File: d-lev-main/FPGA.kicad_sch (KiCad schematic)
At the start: 24 parts, among them J2 Tag-Connect TC2030-NL, SW10 SW_Push, SW9 SW_Push, U2 25LCxxx, U3 AC608

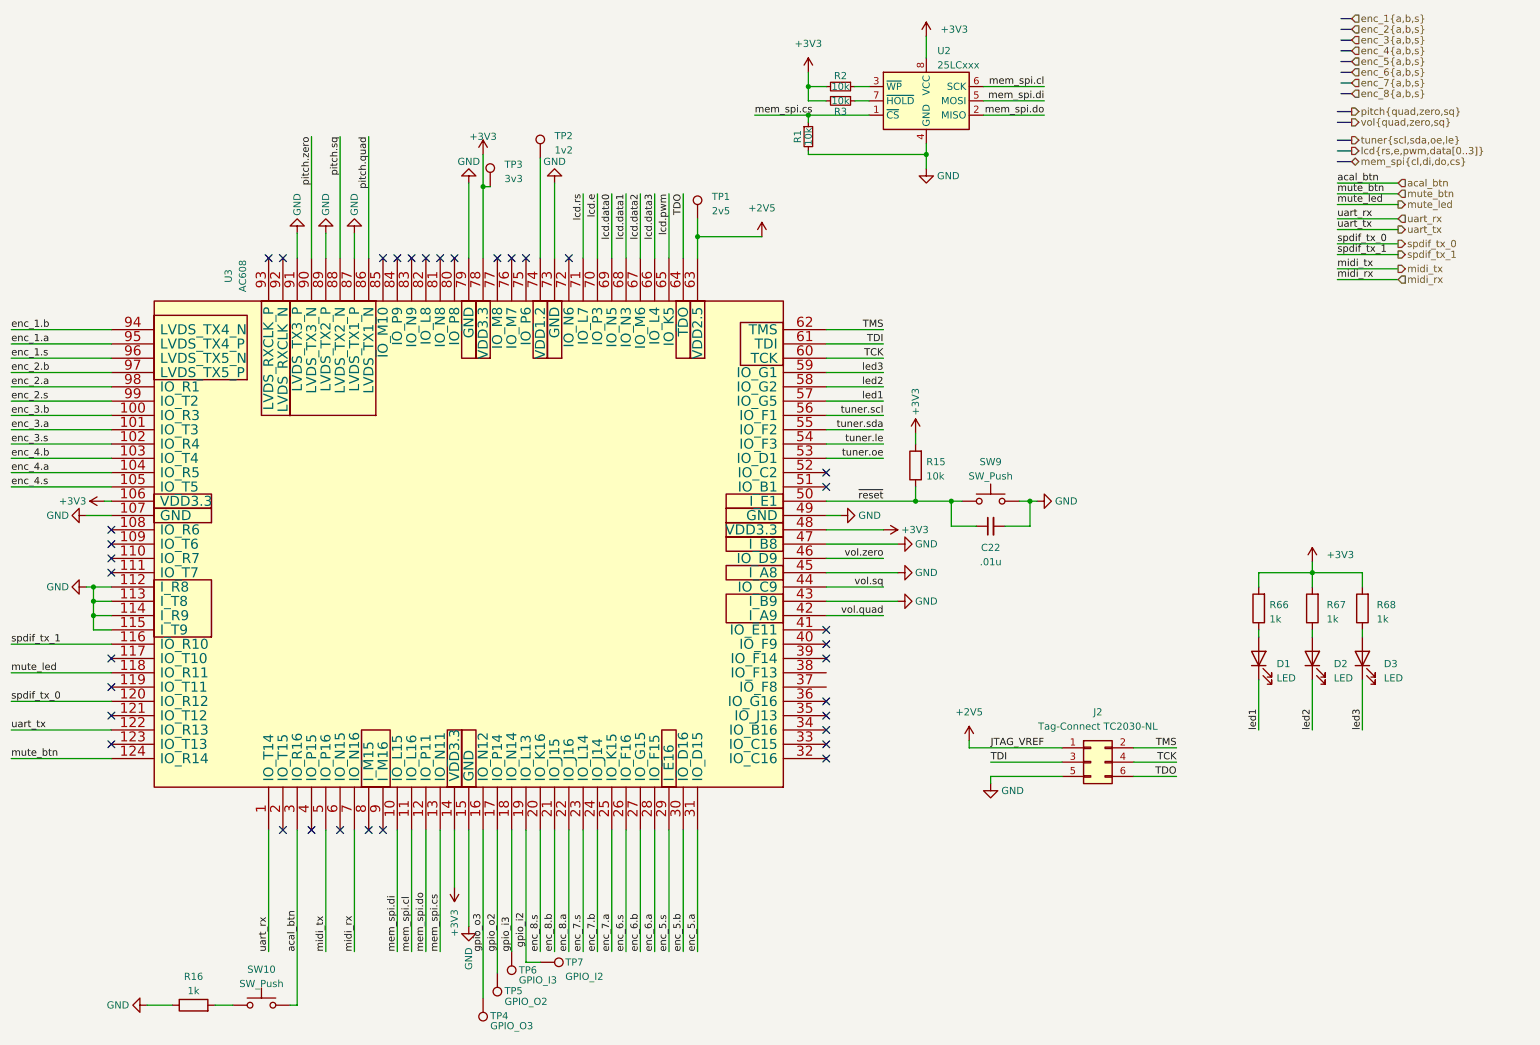
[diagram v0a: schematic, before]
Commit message: round tracks and teardrops
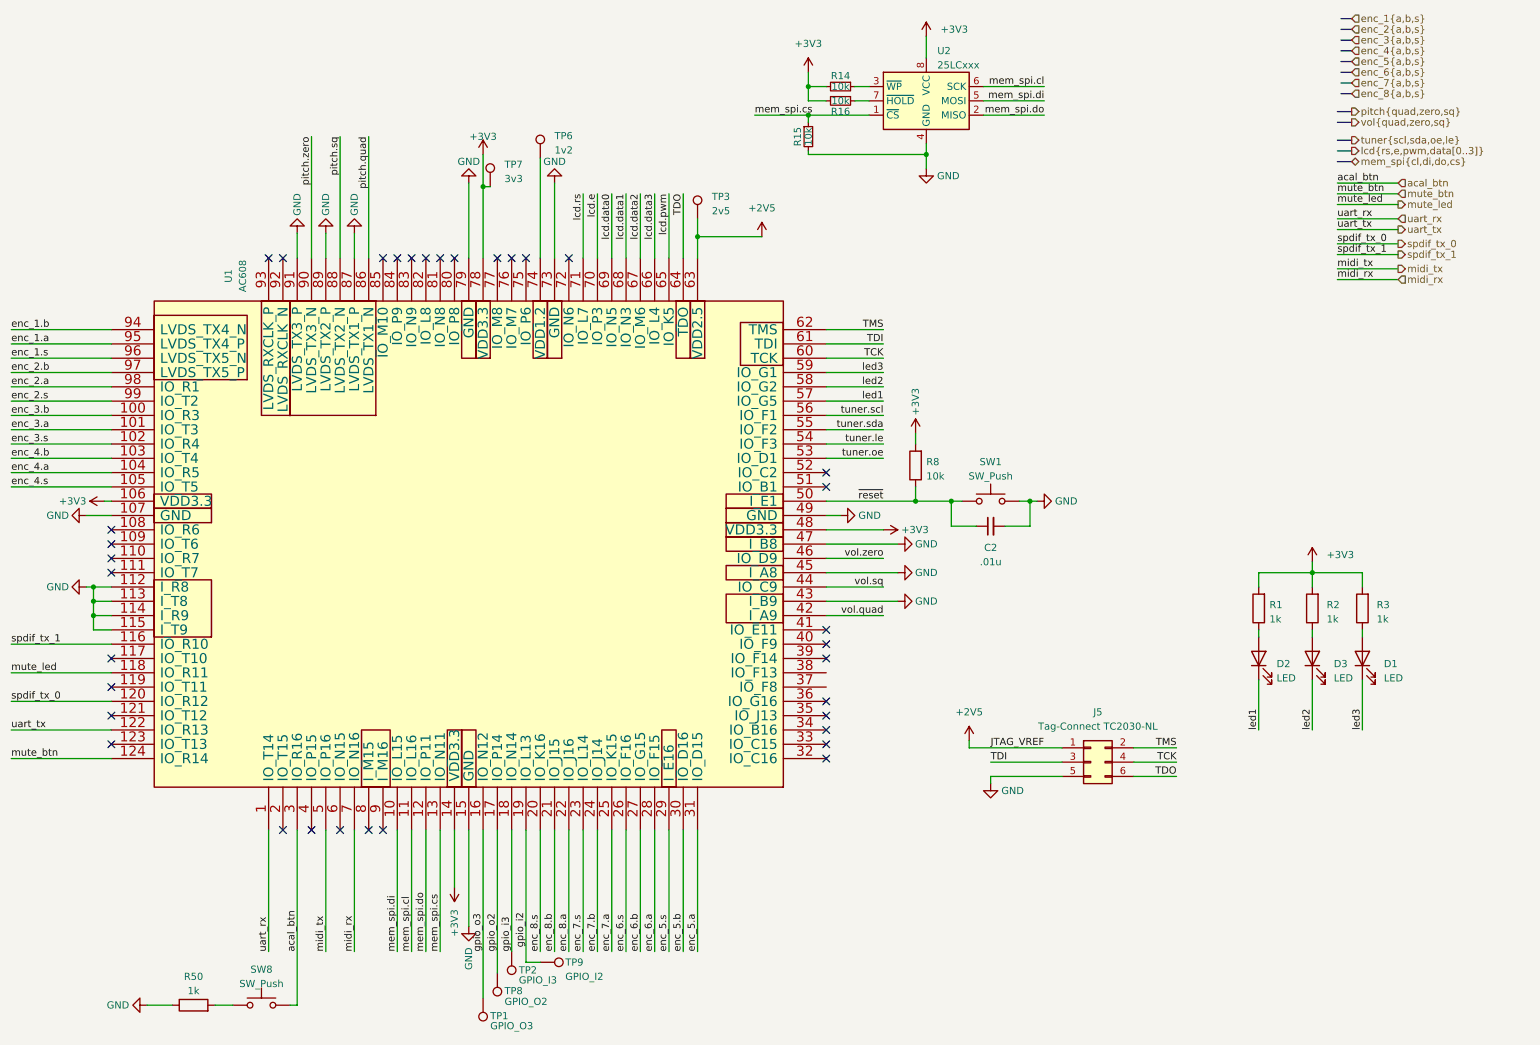
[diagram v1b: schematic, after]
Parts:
- renumbered C22 to C2, D3 to D1, D1 to D2, D2 to D3, J2 to J5, R66 to R1, R2 to R14, R1 to R15, R3 to R16, R67 to R2, R68 to R3, R16 to R50, R15 to R8, SW9 to SW1, SW10 to SW8, TP4 to TP1, TP6 to TP2, TP1 to TP3, TP2 to TP6, TP3 to TP7, TP5 to TP8, TP7 to TP9, U3 to U1

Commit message: many board updates
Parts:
- removed R50: 1k, Resistor_SMD:R_0603_1608Metric, symbol Device:R
- removed SW8: SW_Push, Button_Switch_SMD:SW_SPST_B3U-1000P, symbol Switch:SW_Push
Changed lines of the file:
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@@
-    (stroke (width 0) (type default))
-  )
-  (wire (pts (xy 43.18 191.77) (xy 47.625 191.77))
     (stroke (width 0) (type default))
   )
@@
     (stroke (width 0) (type default))
   )
-  (wire (pts (xy 69.85 191.77) (xy 69.85 160.655))
+  (wire (pts (xy 69.85 182.245) (xy 69.85 160.655))
     (stroke (width 0) (type default))
   )
@@
     (stroke (width 0) (type default))
   )
-  (wire (pts (xy 68.58 191.77) (xy 69.85 191.77))
-    (stroke (width 0) (type default))
-  )
   (wire (pts (xy 19.05 142.875) (xy 36.83 142.875))
     (stroke (width 0) (type default))
@@
   )
   (wire (pts (xy 80.01 59.055) (xy 80.01 54.61))
-    (stroke (width 0) (type default))
-  )
-  (wire (pts (xy 55.245 191.77) (xy 58.42 191.77))
     (stroke (width 0) (type default))
   )
@@
         (path "/eb5e8bfd-9871-4528-bf57-58851bf63907/acdfb54c-8449-4fbe-9778-47a925c872ef"
           (reference "TP8") (unit 1)
-        )
-      )
-    )
-  )
-  (symbol (lib_id "Switch:SW_Push") (at 63.5 191.77 0) (mirror y) (unit 1)
-    (in_bom yes) (on_board yes) (dnp no)
-    (property "Reference" "SW8" (at 63.5 185.42 0)
-      (effects (font (size 1.27 1.27)))
-    )
-    (property "Value" "SW_Push" (at 63.5 187.96 0)
-      (effects (font (size 1.27 1.27)))
-    )
-    (property "Footprint" "Button_Switch_SMD:SW_SPST_B3U-1000P" (at 63.5 186.69 0)
-      (effects (font (size 1.27 1.27)) hide)
-    )
-    (property "Datasheet" "~" (at 63.5 186.69 0)
-      (effects (font (size 1.27 1.27)) hide)
-    )
-    (pin "1")
-    (pin "2")
-    (instances
-      (project "dlev-mini"
-        (path "/eb5e8bfd-9871-4528-bf57-58851bf63907/acdfb54c-8449-4fbe-9778-47a925c872ef"
-          (reference "SW8") (unit 1)
         )
       )
@@
     )
   )
-  (symbol (lib_id "Device:R") (at 51.435 191.77 90) (unit 1)
-    (in_bom yes) (on_board yes) (dnp no) (fields_autoplaced)
-    (property "Reference" "R50" (at 51.435 186.69 90)
-      (effects (font (size 1.27 1.27)))
-    )
-    (property "Value" "1k" (at 51.435 189.23 90)
-      (effects (font (size 1.27 1.27)))
-    )
-    (property "Footprint" "Resistor_SMD:R_0603_1608Metric" (at 51.435 193.548 90)
-      (effects (font (size 1.27 1.27)) hide)
-    )
-    (property "Datasheet" "~" (at 51.435 191.77 0)
-      (effects (font (size 1.27 1.27)) hide)
-    )
-    (pin "1")
-    (pin "2")
-    (instances
-      (project "dlev-mini"
-        (path "/eb5e8bfd-9871-4528-bf57-58851bf63907/acdfb54c-8449-4fbe-9778-47a925c872ef"
-          (reference "R50") (unit 1)
-        )
-      )
-    )
-  )
   (symbol (lib_id "Connector:TestPoint") (at 140.97 52.07 0) (unit 1)
     (in_bom yes) (on_board yes) (dnp no) (fields_autoplaced)
@@
         )
       )
-    )
-  )
-  (symbol (lib_id "power:GND") (at 43.18 191.77 270) (mirror x) (unit 1)
-    (in_bom yes) (on_board yes) (dnp no)
-    (property "Reference" "#PWR041" (at 36.83 191.77 0)
-      (effects (font (size 1.27 1.27)) hide)
-    )
-    (property "Value" "GND" (at 40.005 191.77 90)
-      (effects (font (size 1.27 1.27)) (justify right))
-    )
-    (property "Footprint" "" (at 43.18 191.77 0)
-      (effects (font (size 1.27 1.27)) hide)
-    )
-    (property "Datasheet" "" (at 43.18 191.77 0)
-      (effects (font (size 1.27 1.27)) hide)
-    )
-    (pin "1")
-    (instances
-      (project "dlev-mini"
-        (path "/eb5e8bfd-9871-4528-bf57-58851bf63907/acdfb54c-8449-4fbe-9778-47a925c872ef"
-          (reference "#PWR041") (unit 1)
-        )
-      )

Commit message: Add iBOMs and additional part numbers
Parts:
- C2: value .01u -> 10n; MPN (none) -> C0603C103K2RECAUTO; Notes (none) -> Common, can substitute for cheaper; Supplier (none) -> Mouser; Supplier URL (none) -> https://www.mouser.com/ProductDetail/80-C0603C103K2REAUTO
- D1, D2, D3: Supplier (none) -> Mouser; Supplier URL (none) -> https://www.mouser.com/ProductDetail/Wurth-Elektronik/15006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
- J5: DNP (none) -> Y; now left out of the parts list
- SW1: Supplier (none) -> Mouser; Supplier URL (none) -> https://www.mouser.com/ProductDetail/Omron-Electronics/B3U-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
- TP1: value GPIO_O3 -> TestPoint; DNP (none) -> Y; now left out of the parts list
- TP2: value GPIO_I3 -> TestPoint; DNP (none) -> Y; now left out of the parts list
- TP3: value 2v5 -> TestPoint; DNP (none) -> Y; now left out of the parts list
- TP6: value 1v2 -> TestPoint; DNP (none) -> Y; now left out of the parts list
- TP7: value 3v3 -> TestPoint; DNP (none) -> Y; now left out of the parts list
- TP8: value GPIO_O2 -> TestPoint; DNP (none) -> Y; now left out of the parts list
- TP9: value GPIO_I2 -> TestPoint; DNP (none) -> Y; now left out of the parts list
- U1: Supplier (none) -> Taobao; Supplier Alt URL (none) -> https://www.aliexpress.us/item/3256805040800929.htm; Supplier URL (none) -> https://item.taobao.com/item.htm?spm=a312a.7700824.w4004-16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
- U2: value 25LCxxx -> 25LC1024; Supplier (none) -> Mouser; Supplier URL (none) -> https://www.mouser.com/ProductDetail/Microchip-Technology/2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
